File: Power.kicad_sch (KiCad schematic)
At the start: 8 parts, among them U1 AMS1117-3.3, U2 NE5532

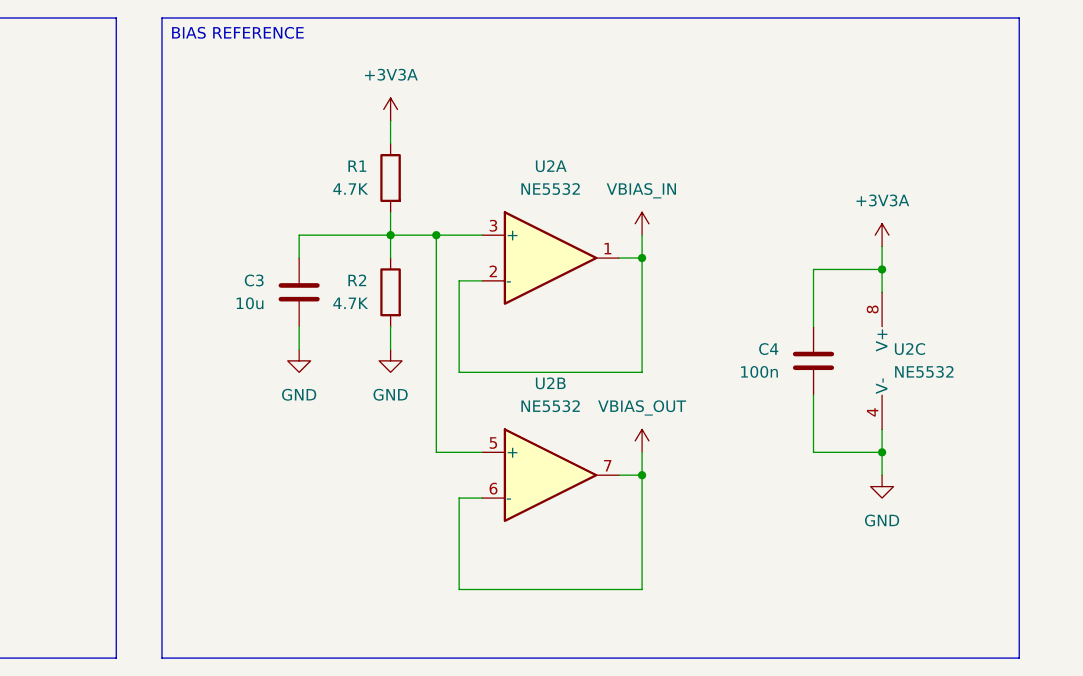
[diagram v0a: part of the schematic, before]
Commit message: Schematic
Updated the schematic.
Added the codec schematic module.
Added the buffer schematic module.
Added the RP2350 schematic module.
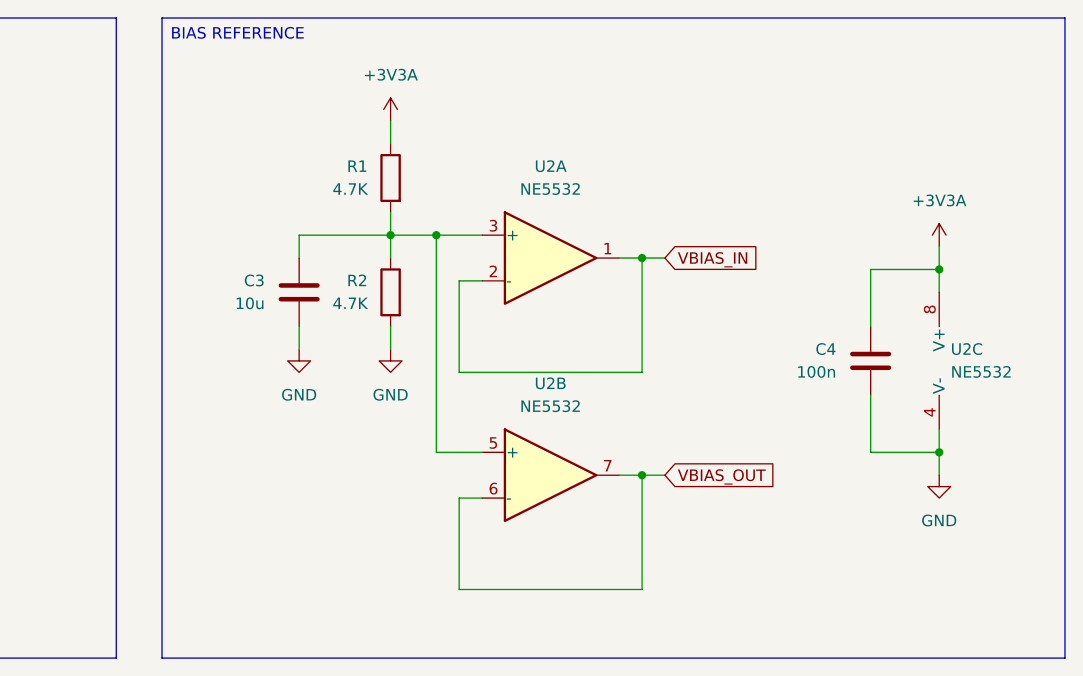
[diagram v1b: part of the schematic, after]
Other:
- moved on the sheet: C4, U2C

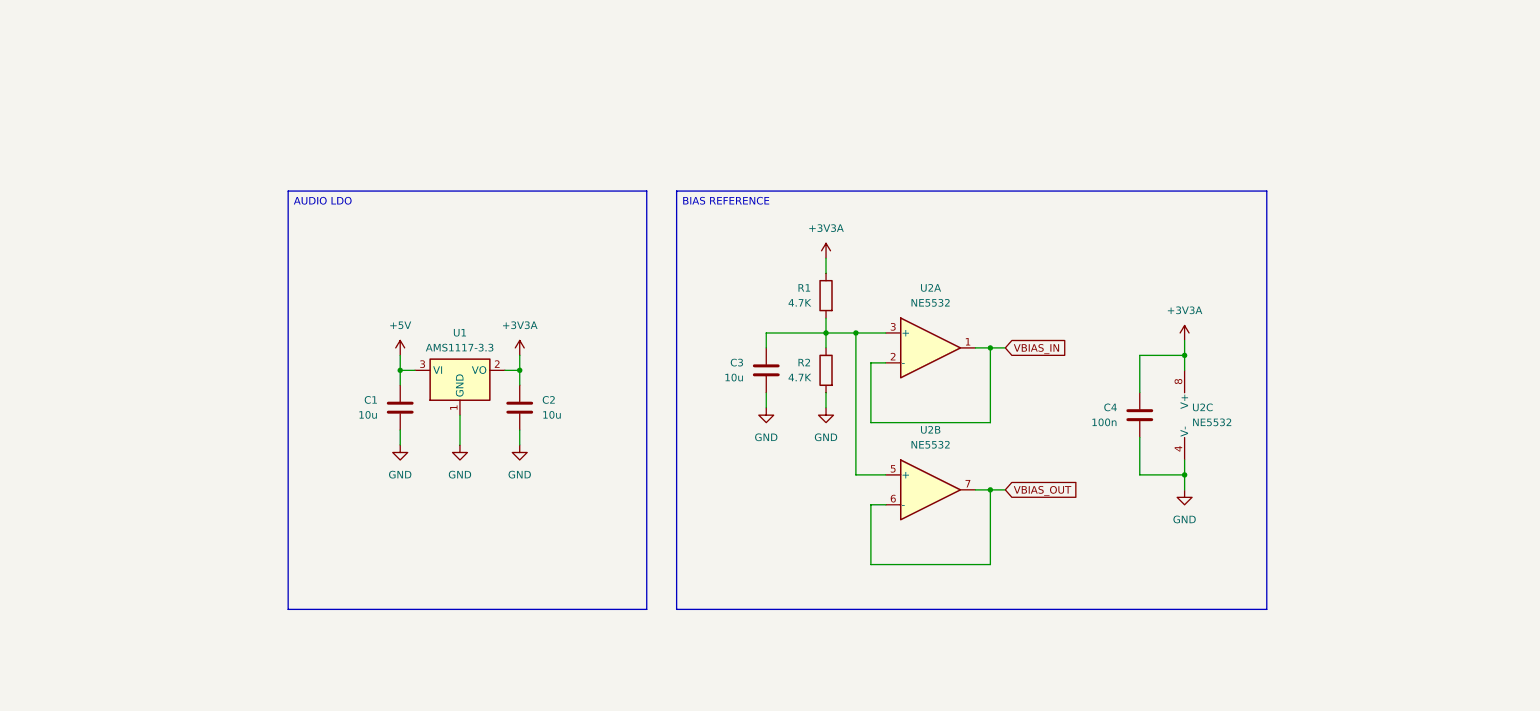
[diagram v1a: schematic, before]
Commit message: Schematic
Updated the power delivery module.
Other minor changes.
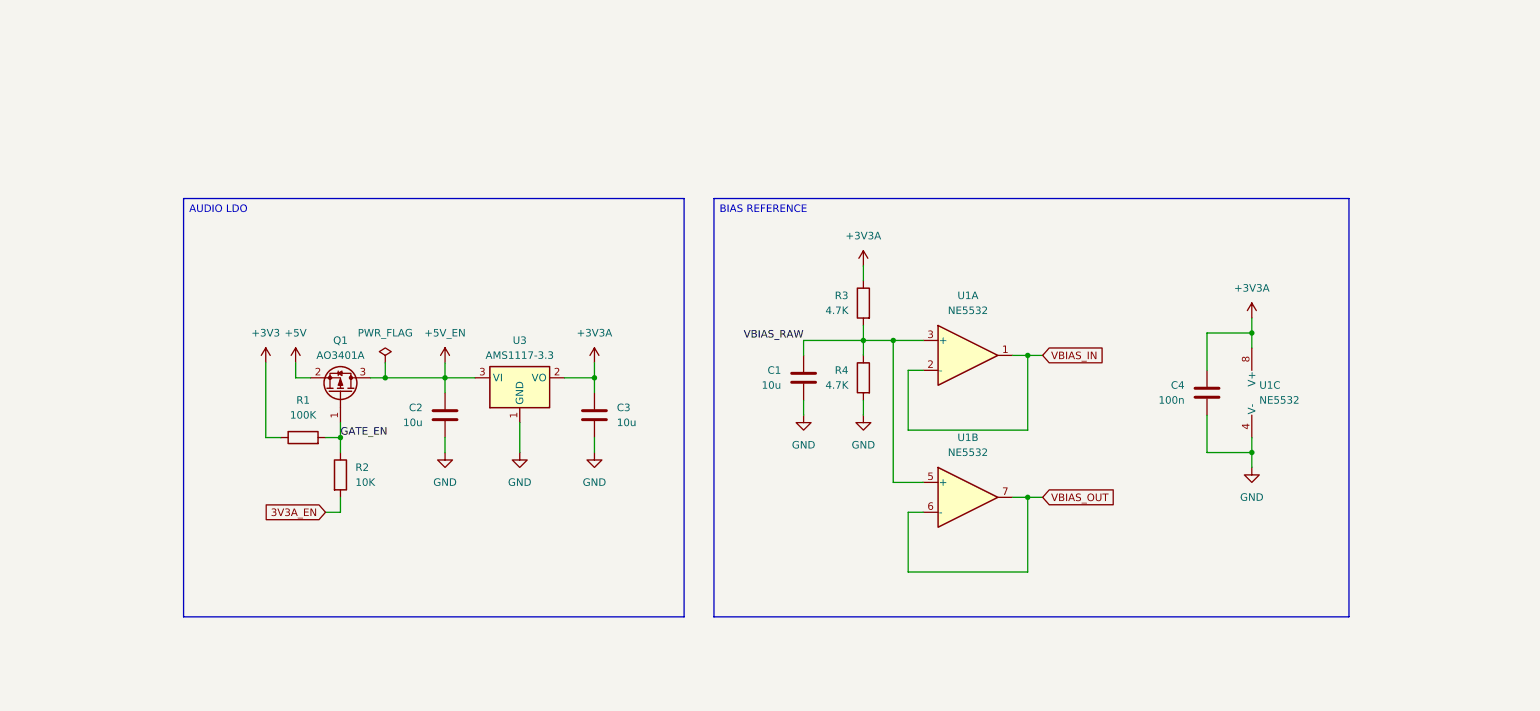
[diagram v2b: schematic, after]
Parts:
- removed U1: AMS1117-3.3, Package_TO_SOT_SMD:SOT-223-3_TabPin2, symbol Regulator_Linear:AMS1117-3.3
- added Q1: AO3401A, Package_TO_SOT_SMD:SOT-23, symbol Transistor_FET:Q_PMOS_GSD
- added R1: 100K, Resistor_SMD:R_0603_1608Metric, symbol Device:R
- added R2: 10K, Resistor_SMD:R_0603_1608Metric, symbol Device:R
- added U3: AMS1117-3.3, Package_TO_SOT_SMD:SOT-223-3_TabPin2, symbol Regulator_Linear:AMS1117-3.3
- renumbered C3 to C1, C1 to C2, C2 to C3, R1 to R3, R2 to R4, U2 to U1
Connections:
- net +3V3A: now also U3.2 (VO)
- net +5V: now also Q1.2 (S); no longer C2.1
- net GND: now also U3.1 (GND)
- net VBIAS_RAW: now reaches C1.1, R3.2, R4.1, U1.3 (+), U1.5 (+)
- new net +3V3: R1.1
- new net +5V_EN: C2.1, Q1.3 (D), U3.3 (VI)
- new net 3V3A_EN: R2.2
- new net GATE_EN: Q1.1 (G), R1.2, R2.1
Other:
- company: (none) -> DavidMolTor
- title: (none) -> SIMPLE CODEC
- moved on the sheet: C1, C2, C3, C4, R3, R4, U1A, U1B, U1C

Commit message: Moved to a CS4272 codec as a cheaper alternative with similar performance.
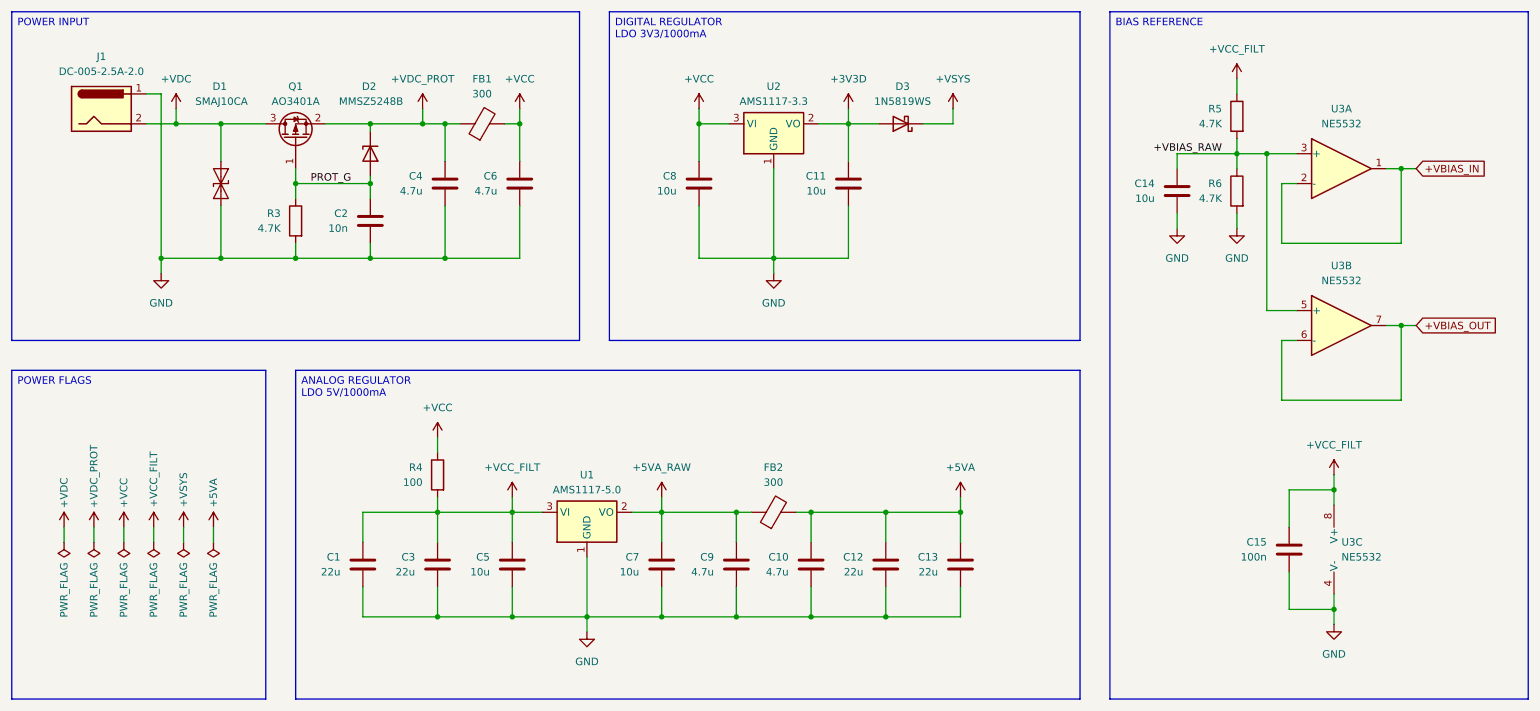
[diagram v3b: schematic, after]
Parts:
- removed Q1: AO3401A, Package_TO_SOT_SMD:SOT-23, symbol Transistor_FET:Q_PMOS_GSD
- removed R1: 100K, Resistor_SMD:R_0603_1608Metric, symbol Device:R
- removed R2: 10K, Resistor_SMD:R_0603_1608Metric, symbol Device:R
- removed U3: AMS1117-3.3, Package_TO_SOT_SMD:SOT-223-3_TabPin2, symbol Regulator_Linear:AMS1117-3.3
- added C1, C12, C13, C3: 22u, Capacitor_SMD:C_1206_3216Metric, symbol Device:C
- added C10, C4, C6, C9: 4.7u, Capacitor_SMD:C_1206_3216Metric, symbol Device:C
- added C11, C8: 10u, Capacitor_SMD:C_1206_3216Metric, symbol Device:C
- added C2: 10n, Capacitor_SMD:C_0603_1608Metric, symbol Device:C
- added D1: SMAJ10CA, Diode_SMD:D_SMA, symbol Diode:SMAJ10CA
- added D2: MMSZ5248B, Diode_SMD:D_SOD-123, symbol Device:D_Zener
- added D3: 1N5819WS, Diode_SMD:D_SOD-323, symbol Device:D_Schottky
- added FB1, FB2: 300, Inductor_SMD:L_0805_2012Metric, symbol Device:FerriteBead
- added J1: DC-005-2.5A-2.0, Custom_Parts:BARREL_JACK_HORIZONTAL, symbol Connector:Jack-DC
- added Q1: AO3401A, Package_TO_SOT_SMD:SOT-23, symbol Transistor_FET:AO3401A
- added R3: 4.7K, Resistor_SMD:R_0603_1608Metric, symbol Device:R
- added R4: 100, Resistor_SMD:R_0603_1608Metric, symbol Device:R
- added U1: AMS1117-5.0, Package_TO_SOT_SMD:SOT-223-3_TabPin2, symbol Regulator_Linear:AMS1117-5.0
- added U2: AMS1117-3.3, Package_TO_SOT_SMD:SOT-223-3_TabPin2, symbol Regulator_Linear:AMS1117-3.3
- renumbered C1 to C14, C4 to C15, C2 to C5, C3 to C7, R3 to R5, R4 to R6, U1 to U3
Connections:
- net +5V_EN is gone; now on net +VCC_FILT: C5.1
- net GND: now also C1.2, C10.2, C11.2, C12.2, C13.2, C2.2, C3.2, C4.2, C6.2, C8.2, C9.2, D1.2 (A2), J1.1, R3.2, U1.1 (GND), U2.1 (GND)
- net +3V3A renamed +VCC_FILT
- net +VCC_FILT: now also C1.1, C3.1, R4.2, U1.3 (VI); no longer C7.1
- net VBIAS_IN renamed +VBIAS_IN
- net VBIAS_OUT renamed +VBIAS_OUT
- net VBIAS_RAW renamed +VBIAS_RAW
- new net +3V3D: C11.1, D3.2 (A), U2.2 (VO)
- new net +5VA: C10.1, C12.1, C13.1, FB2.2
- new net +5VA_RAW: C7.1, C9.1, FB2.1, U1.2 (VO)
- new net +VCC: C6.1, C8.1, FB1.2, R4.1, U2.3 (VI)
- new net +VDC: D1.1 (A1), J1.2, Q1.3 (D)
- new net +VDC_PROT: C4.1, D2.1 (K), FB1.1, Q1.2 (S)
- new net +VSYS: D3.1 (K)
- new net PROT_G: C2.1, D2.2 (A), Q1.1 (G), R3.1
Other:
- moved on the sheet: C14, C15, C5, C7, R5, R6, U3A, U3B, U3C

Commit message: Initial layout
Initial layout inside a 1590N1/125B pedal enclosure.
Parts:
- removed J1: DC-005-2.5A-2.0, Custom_Parts:BARREL_JACK_HORIZONTAL, symbol Connector:Jack-DC
- added X1: PEDAL_COMBO_TOP, Custom_Parts:PEDAL_COMBO_TOP, symbol Custom_Parts:PEDAL_COMBO_TOP
- renumbered R3 to R4, R4 to R5, R5 to R6, R6 to R7
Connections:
- net +VDC: now also X1.2
- net GND: now also X1.1

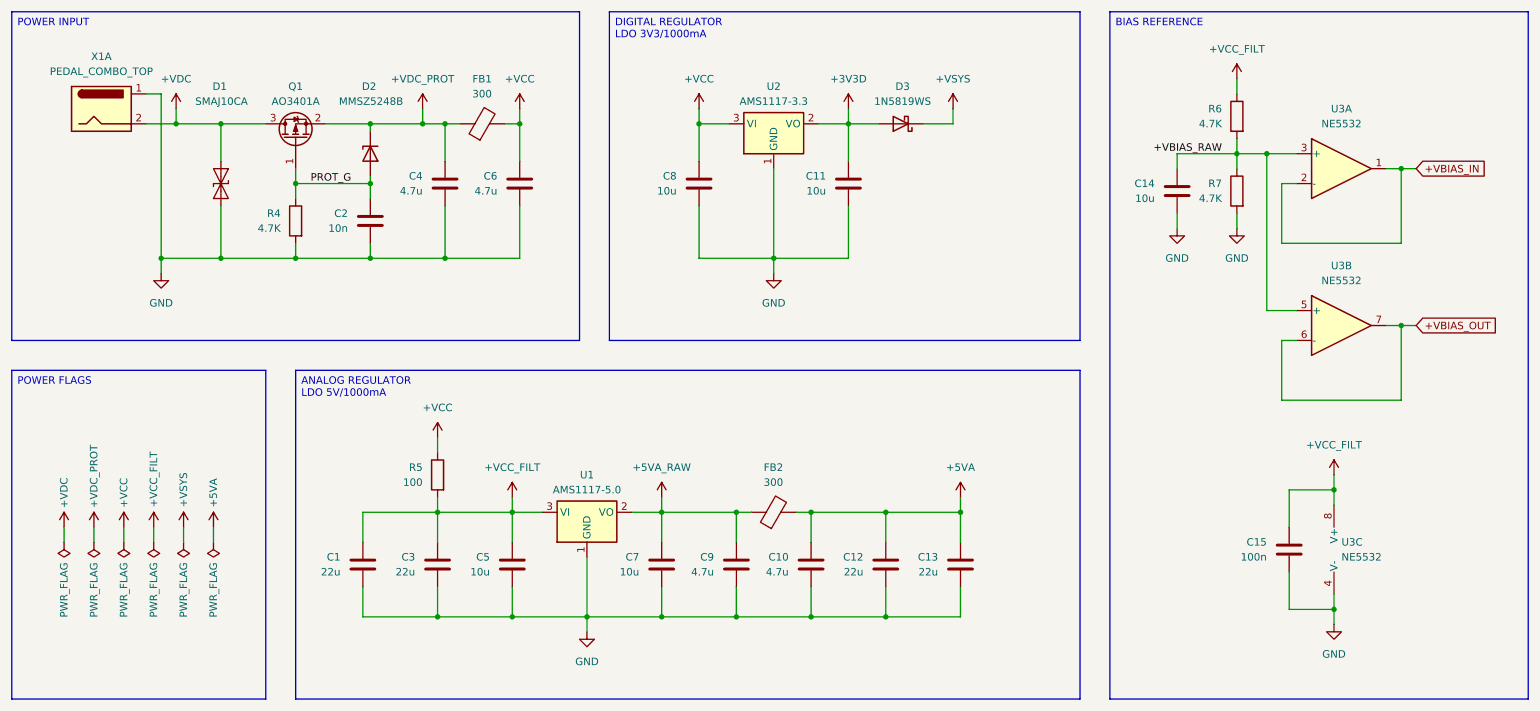
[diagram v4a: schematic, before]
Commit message: RP2350 layout
Updated the layout for the RP2350.
Added board headers.
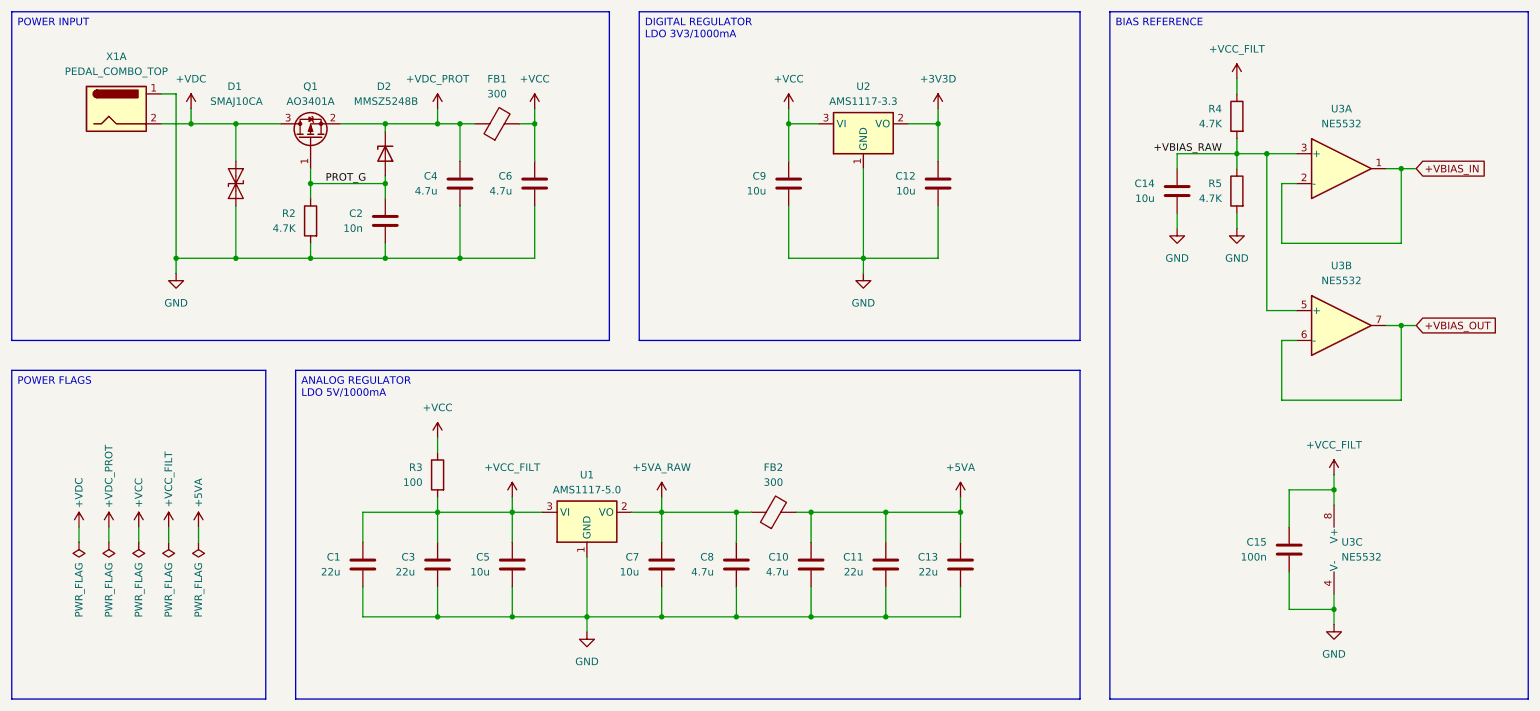
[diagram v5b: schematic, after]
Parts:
- removed D3: 1N5819WS, Diode_SMD:D_SOD-323, symbol Device:D_Schottky
- renumbered C12 to C11, C11 to C12, C9 to C8, C8 to C9, R4 to R2, R5 to R3, R6 to R4, R7 to R5
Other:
- moved on the sheet: C12, C2, C4, C6, C9, D1, D2, FB1, Q1, R2, U2, X1A
